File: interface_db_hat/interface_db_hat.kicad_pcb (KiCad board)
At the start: 4 copper layers, 65 x 56 mm, 88 parts, among them J1 GPIO, J10 Conn_02x06_Counter_Clockwise, J2 DF19G-20P-1H52, J3 Conn_02x06_Counter_Clockwise, J4 Conn_Coaxial_Small, J5 Conn_01x04_Pin, J6 Conn_01x04_Pin, J8 Conn_01x03_Pin, J9 Conn_02x06_Counter_Clockwise, Q1 BC817, U1 MAX-M10M-00B, U2 TCA9617ADGKR, U7 MCP23017x-x-SO

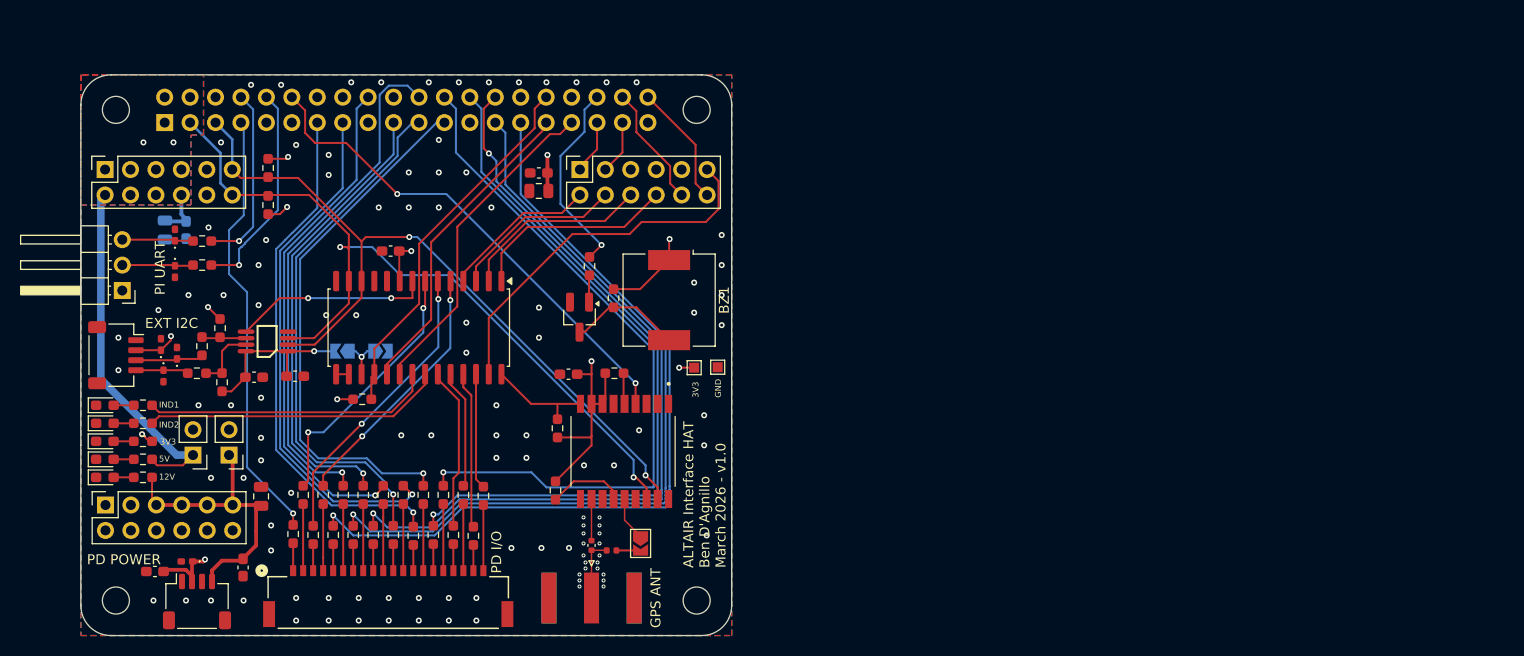
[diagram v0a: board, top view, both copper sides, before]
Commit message: starting interface layout
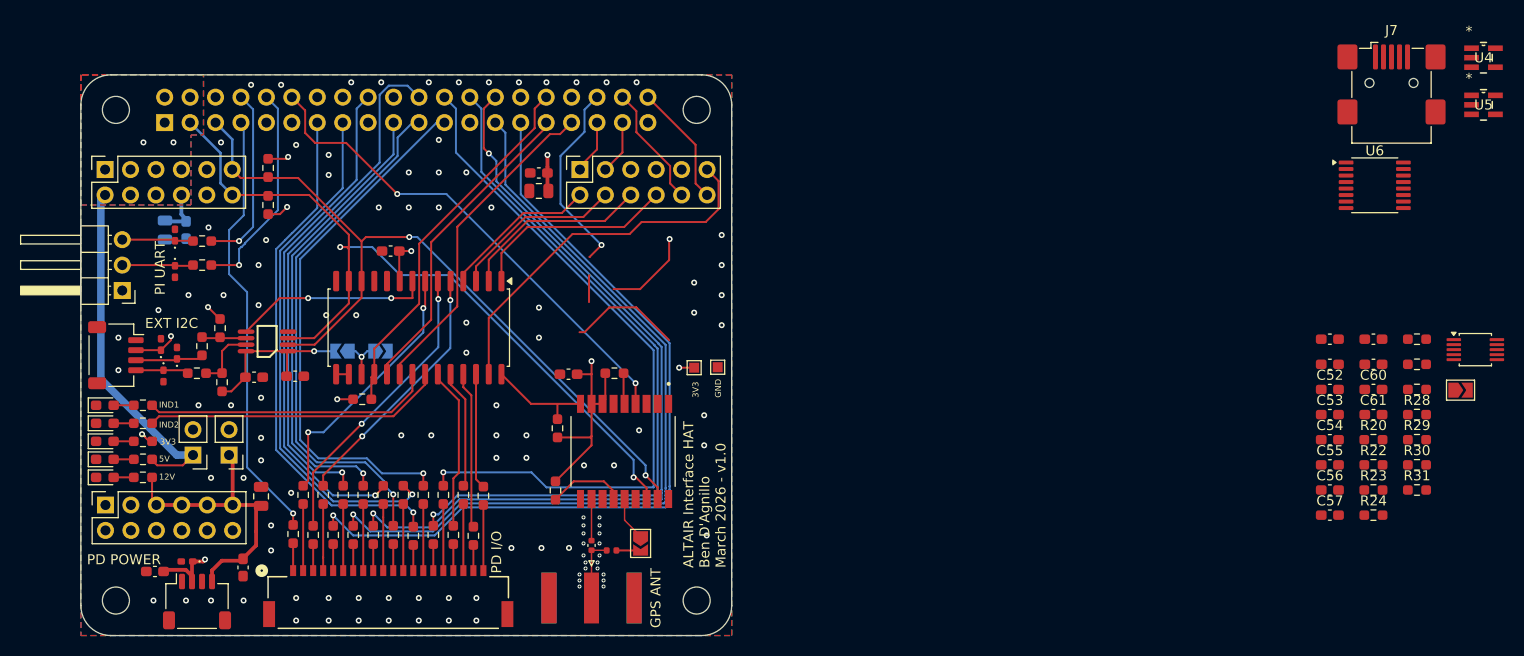
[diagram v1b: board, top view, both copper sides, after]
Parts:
- removed BZ1: Buzzer, Buzzer_Beeper:Buzzer_CUI_CPT-9019S-SMT
- removed Q1: BC817, Package_TO_SOT_SMD:SOT-23_Handsoldering
- removed R15, R17: 330, Resistor_SMD:R_0603_1608Metric_Pad0.98x0.95mm_HandSolder
- added C50: 100nF, Capacitor_SMD:C_0603_1608Metric_Pad1.08x0.95mm_HandSolder, F.Cu at (224.7, 70.4)
- added C51: 100nF, Capacitor_SMD:C_0603_1608Metric_Pad1.08x0.95mm_HandSolder, F.Cu at (224.7, 72.9)
- added C52: 100nF, Capacitor_SMD:C_0603_1608Metric_Pad1.08x0.95mm_HandSolder, F.Cu at (224.7, 75.4)
- added C53: 100nF, Capacitor_SMD:C_0603_1608Metric_Pad1.08x0.95mm_HandSolder, F.Cu at (224.7, 77.9)
- added C54: 1nF, Capacitor_SMD:C_0603_1608Metric_Pad1.08x0.95mm_HandSolder, F.Cu at (224.7, 80.4)
- added C55: 330pF, Capacitor_SMD:C_0603_1608Metric_Pad1.08x0.95mm_HandSolder, F.Cu at (224.7, 83.0)
- added C56: 100pF, Capacitor_SMD:C_0603_1608Metric_Pad1.08x0.95mm_HandSolder, F.Cu at (224.7, 85.5)
- added C57: 33pF, Capacitor_SMD:C_0603_1608Metric_Pad1.08x0.95mm_HandSolder, F.Cu at (224.7, 88.0)
- added C58: 1nF, Capacitor_SMD:C_0603_1608Metric_Pad1.08x0.95mm_HandSolder, F.Cu at (229.1, 70.4)
- added C59: 330pF, Capacitor_SMD:C_0603_1608Metric_Pad1.08x0.95mm_HandSolder, F.Cu at (229.1, 72.9)
- added C60: 100pF, Capacitor_SMD:C_0603_1608Metric_Pad1.08x0.95mm_HandSolder, F.Cu at (229.1, 75.4)
- added C61: 33pF, Capacitor_SMD:C_0603_1608Metric_Pad1.08x0.95mm_HandSolder, F.Cu at (229.1, 77.9)
- added J7: USB_B_Mini, Connector_USB:USB_Mini-B_Wuerth_65100516121_Horizontal, F.Cu at (230.9, 44.8)
- added JP9: SolderJumper_2_Open, Jumper:SolderJumper-2_P1.3mm_Open_TrianglePad1.0x1.5mm, F.Cu at (237.8, 75.5)
- added R20: 50, Resistor_SMD:R_0603_1608Metric_Pad0.98x0.95mm_HandSolder, F.Cu at (229.1, 80.4)
- added R22: 100, Resistor_SMD:R_0603_1608Metric_Pad0.98x0.95mm_HandSolder, F.Cu at (229.1, 83.0)
- added R23: 1k, Resistor_SMD:R_0603_1608Metric_Pad0.98x0.95mm_HandSolder, F.Cu at (229.1, 85.5)
- added R24: 0, Resistor_SMD:R_0603_1608Metric_Pad0.98x0.95mm_HandSolder, F.Cu at (229.1, 88.0)
- added R25: 0, Resistor_SMD:R_0603_1608Metric_Pad0.98x0.95mm_HandSolder, F.Cu at (233.4, 70.4)
- added R26: 10k, Resistor_SMD:R_0603_1608Metric_Pad0.98x0.95mm_HandSolder, F.Cu at (233.4, 72.9)
- added R27: 100k, Resistor_SMD:R_0603_1608Metric_Pad0.98x0.95mm_HandSolder, F.Cu at (233.4, 75.4)
- added R28: 100, Resistor_SMD:R_0603_1608Metric_Pad0.98x0.95mm_HandSolder, F.Cu at (233.4, 77.9)
- added R29: 1k, Resistor_SMD:R_0603_1608Metric_Pad0.98x0.95mm_HandSolder, F.Cu at (233.4, 80.4)
- added R30: 10k, Resistor_SMD:R_0603_1608Metric_Pad0.98x0.95mm_HandSolder, F.Cu at (233.4, 83.0)
- added R31: 100k, Resistor_SMD:R_0603_1608Metric_Pad0.98x0.95mm_HandSolder, F.Cu at (233.4, 85.5)
- added U3: ADS1115IDGS, Package_SO:TSSOP-10_3x3mm_P0.5mm, F.Cu at (239.3, 71.4)
- added U4: OPA320AIDBVR, OPA320:DBV5, F.Cu at (240.1, 42.3)
- added U5: OPA320AIDBVR, OPA320:DBV5, F.Cu at (240.1, 47.0)
- added U6: TMUX1209PWR, Package_SO:TSSOP-16_4.4x5mm_P0.65mm, F.Cu at (229.2, 55.0)
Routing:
- net (no net): track 0.00 -> 14.0 mm
- net Net-(BZ1--): track 11.3 -> 0.00 mm
- net Net-(Q1-B): track 2.71 -> 0.00 mm

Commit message: interface layout done
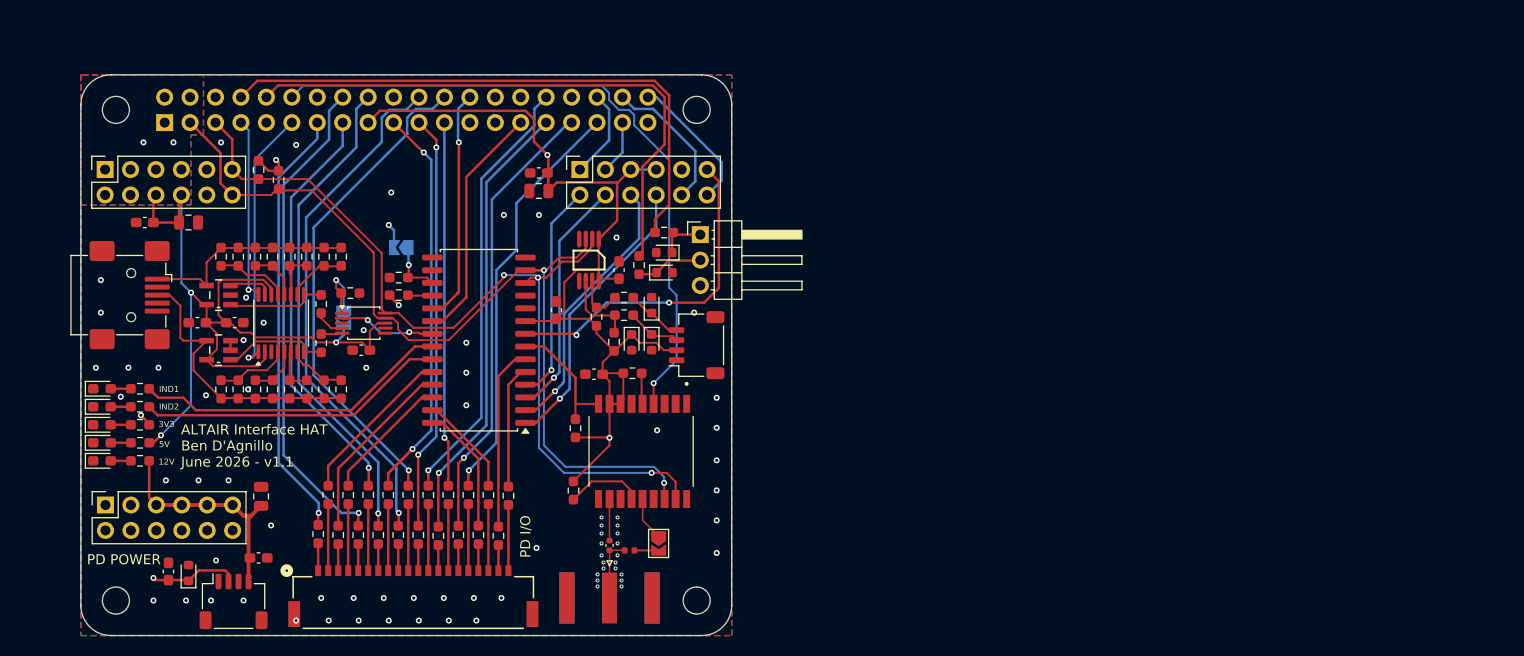
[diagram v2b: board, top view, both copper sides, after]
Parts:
- removed C4, C53: 100nF, Capacitor_SMD:C_0603_1608Metric_Pad1.08x0.95mm_HandSolder
- removed JP8: SolderJumper_2_Open, Jumper:SolderJumper-2_P1.3mm_Open_TrianglePad1.0x1.5mm
- removed TP1, TP2: TestPoint_2Pole, Connector_PinHeader_2.54mm:PinHeader_1x02_P2.54mm_Vertical
- removed TP3, TP4: TestPoint, TestPoint:TestPoint_Pad_1.0x1.0mm
- added R13: 10k, Resistor_SMD:R_0603_1608Metric_Pad0.98x0.95mm_HandSolder, F.Cu at (131.8, 64.2)
- C33, C34: moved to F.Cu
- C54, C55, C56, C57, C58, C59, C60, C61: footprint Capacitor_SMD:C_0603_1608Metric_Pad1.08x0.95mm_HandSolder -> Resistor_SMD:R_0603_1608Metric_Pad0.98x0.95mm_HandSolder
- D10, D36, D37, D38, D47, D48: footprint Diode_SMD:D_0402_1005Metric_Pad0.77x0.64mm_HandSolder -> Diode_SMD:D_0603_1608Metric
- JP9: moved to B.Cu
- moved U4 129.7 mm to (113.8, 71.5), turned to 180 degrees
- moved U5 127.7 mm to (113.8, 66.0), turned to 180 degrees
- moved J7 127.6 mm to (105.0, 66.0), turned to -90 degrees
- moved R28 118.8 mm to (115.7, 62.2), turned to -90 degrees
- moved R29 115.7 mm to (119.1, 62.2), turned to -90 degrees
- moved C58 115.4 mm to (114.0, 62.2), turned to 90 degrees
- moved R30 114.5 mm to (120.9, 62.2), turned to -90 degrees
- moved R22 113.6 mm to (115.7, 75.4), turned to 90 degrees
- moved C50 113.1 mm to (111.6, 68.8), turned to 180 degrees
- moved R26 112.6 mm to (120.9, 75.4), turned to 90 degrees
- moved C59 112.2 mm to (117.4, 62.2), turned to 90 degrees
- moved JP9 111.8 mm to (126.2, 68.3), turned to -90 degrees
- moved U3 111.0 mm to (128.2, 68.8)
- moved C54 110.9 mm to (114.0, 75.4), turned to -90 degrees
- moved R23 110.4 mm to (119.1, 75.4), turned to 90 degrees
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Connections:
- C55 pad 2: /photodiode/RC2_IN -> /photodiode/PDA_ANODE
- C56 pad 2: /photodiode/RC2_IN -> /photodiode/PDA_ANODE
- C57 pad 2: /photodiode/RC2_IN -> /photodiode/PDA_ANODE
- C59 pad 2: /photodiode/RC2_IN -> /photodiode/PDB_ANODE
- C60 pad 2: /photodiode/RC2_IN -> /photodiode/PDB_ANODE
- C61 pad 2: /photodiode/RC2_IN -> /photodiode/PDB_ANODE
- J1 pad 11: /HAT_connections/GPIO17 -> /MUX_A0
- J1 pad 13: /SPI_CS4 -> /INT_SLCTA
- J1 pad 15: /SPI_CS3 -> /~{DRDY1}
- J1 pad 16: /HAT_connections/GPIO23 -> /INT_SLCTB
- J1 pad 18: /STRT2 -> /~{DRDY2}
- J1 pad 22: /~{DRDY1} -> /STRT1
- J1 pad 24: /SPI_CS2 -> /STRT2
- J1 pad 26: /SPI_CS1 -> /EXP_INT_B
- J1 pad 27: /~{DRDY2} -> /HAT_connections/ID_SDA
- J1 pad 28: /STRT1 -> /HAT_connections/ID_SCL
- J1 pad 29: /INT_SLCTB -> /EXP_INT_A
- J1 pad 31: /HAT_connections/EXP_INT_B -> /SPI_CS4
- J1 pad 32: /HAT_connections/GPIO12/PWM0 -> /SPI_CS3
- J1 pad 33: /HAT_connections/EXP_INT_A -> /SPI_CS1
- J1 pad 35: /SERVO_2 -> /SPI_CS2
- J1 pad 36: /BUZZER -> /SERVO_2
- J1 pad 7: /INT_SLCTA -> /MUX_A1
- J7 pad 1: /photodiode/PDA_ANODE -> /photodiode/PDB_ANODE
- J7 pad 3: /photodiode/PDB_ANODE -> /photodiode/PDA_ANODE
- J8 pad 1: GND -> Net-(D48-K)
- J8 pad 3: Net-(D48-K) -> GND
- R23 pad 1: /photodiode/RC2_IN -> /photodiode/PDA_ANODE
- R24 pad 2: /photodiode/PD_OUTA -> /photodiode/PD_OUTB
- R25 pad 1: /photodiode/PD_OUTB -> /photodiode/PD_OUTA
- R26 pad 1: /photodiode/RC2_IN -> /photodiode/PDA_ANODE
- R27 pad 1: /photodiode/RC2_IN -> /photodiode/PDA_ANODE
- R29 pad 1: /photodiode/RC2_IN -> /photodiode/PDB_ANODE
- R30 pad 1: /photodiode/RC2_IN -> /photodiode/PDB_ANODE
- R31 pad 1: /photodiode/RC2_IN -> /photodiode/PDB_ANODE
- R9 pad 1: /HAT_connections/GPIO12/PWM0 -> /HAT_connections/~{IO_EXP_RST}
- U2 pad 5: /HAT_connections/I2CB_EN -> unconnected-(U2-EN-Pad5)
- U3 pad 10: /photodiode/I2C_SCL -> /I2C_SCL
- U3 pad 2: /photodiode/ADC_RDY -> /ADC_RDY
- U3 pad 9: /photodiode/I2C_SDA -> /I2C_SDA
- U6 pad 1: /photodiode/MUX_A0 -> /MUX_A0
- U6 pad 16: /photodiode/MUX_A1 -> /MUX_A1
- U7 pad 18: /HAT_connections/GPIO12/PWM0 -> /HAT_connections/~{IO_EXP_RST}
- U7 pad 19: /HAT_connections/EXP_INT_B -> /EXP_INT_B
- U7 pad 20: /HAT_connections/EXP_INT_A -> /EXP_INT_A
- U7 pad 21: /IND_1 -> /ADC_RDY
- U7 pad 22: /IND_2 -> /IND_1
- U7 pad 23: /IVC_SW_2_SOL -> /IND_2
- U7 pad 24: /IVC_SW_1_SOL -> /~{PD_RESET}
- U7 pad 25: /IVC_SW_1 -> /INT_RST
- U7 pad 26: /IVC_SW_2 -> /INT_HLD
- U7 pad 27: /IND_3 -> /IVC_SW_1_SOL
- U7 pad 28: /~{GPS_RST} -> /IVC_SW_2_SOL
- U7 pad 5: /INT_HLD -> /IVC_SW_2
- U7 pad 6: /INT_RST -> /IVC_SW_1
- U7 pad 7: /~{PD_RESET} -> /~{GPS_RST}
- U7 pad 8: /HAT_connections/I2CB_EN -> /IND_3
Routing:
- net +3V3: track 68.6 -> 120.6 mm, vias 12 -> 7
- net /HAT_connections/GPIO14/TXD0: track 18.2 -> 58.3 mm, vias 1 -> 0
- net /HAT_connections/GPIO12/PWM0: track 37.4 -> 0.00 mm
- net /HAT_connections/GPIO15/RXD0: track 21.7 -> 57.7 mm, vias 1 -> 0
- net /HAT_connections/EXP_INT_A: track 32.8 -> 0.00 mm
- net /HAT_connections/EXP_INT_B: track 31.7 -> 0.00 mm
- net /INT_SLCTB: track 81.0 -> 49.4 mm
- net /~{DRDY2}: track 79.2 -> 49.0 mm
- net /SPI_CS2: track 70.6 -> 41.6 mm
- net /photodiode/PDA_ANODE: track 0.00 -> 28.1 mm
- net /STRT1: track 79.8 -> 52.3 mm, vias 2 -> 1
- net /SPI_CS1: track 71.9 -> 45.1 mm
- net /MUX_A0: track 0.00 -> 26.6 mm, vias 0 -> 1
- net /EXP_INT_A: track 0.00 -> 24.1 mm
- net /EXP_INT_B: track 0.00 -> 23.4 mm, vias 0 -> 1
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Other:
- board text added: "ALTAIR Interface HAT Ben D'Agnillo June 2026 - v1.1"
- board text removed: "ALTAIR Interface HAT Ben D'Agnillo March 2026 - v1.0"
- board text removed: "EXT I2C"
- board text removed: "GND"
- board text removed: "GPS ANT"
- board text removed: "PI UART"

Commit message: fixed interface schematic
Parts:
- C54, C55, C56, C57, C58, C59, C60, C61: footprint Resistor_SMD:R_0603_1608Metric_Pad0.98x0.95mm_HandSolder -> Capacitor_SMD:C_0603_1608Metric_Pad1.08x0.95mm_HandSolder

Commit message: jlc order
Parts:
- removed C50, C51, C52: 100nF, Capacitor_SMD:C_0603_1608Metric_Pad1.08x0.95mm_HandSolder
- removed C54, C58: 1nF, Capacitor_SMD:C_0603_1608Metric_Pad1.08x0.95mm_HandSolder
- removed C55, C59: 330pF, Capacitor_SMD:C_0603_1608Metric_Pad1.08x0.95mm_HandSolder
- removed C56, C60: 100pF, Capacitor_SMD:C_0603_1608Metric_Pad1.08x0.95mm_HandSolder
- removed C57, C61: 33pF, Capacitor_SMD:C_0603_1608Metric_Pad1.08x0.95mm_HandSolder
- removed JP9: SolderJumper_2_Open, Jumper:SolderJumper-2_P1.3mm_Open_TrianglePad1.0x1.5mm
- removed R22, R28: 100, Resistor_SMD:R_0603_1608Metric_Pad0.98x0.95mm_HandSolder
- removed R23, R29: 1k, Resistor_SMD:R_0603_1608Metric_Pad0.98x0.95mm_HandSolder
- removed R24, R25: 0, Resistor_SMD:R_0603_1608Metric_Pad0.98x0.95mm_HandSolder
- removed R26, R30: 10k, Resistor_SMD:R_0603_1608Metric_Pad0.98x0.95mm_HandSolder
- removed R27, R31: 100k, Resistor_SMD:R_0603_1608Metric_Pad0.98x0.95mm_HandSolder
- removed U3: ADS1115IDGS, Package_SO:TSSOP-10_3x3mm_P0.5mm
- removed U4, U5: OPA320AIDBVR, OPA320:DBV5
- removed U6: TMUX1209PWR, Package_SO:TSSOP-16_4.4x5mm_P0.65mm
- added J11: Conn_01x06_Pin, Connector_JST:JST_GH_SM06B-GHS-TB_1x06-1MP_P1.25mm_Horizontal, F.Cu at (104.0, 76.8)
- added R1: 33, Resistor_SMD:R_0603_1608Metric, F.Cu at (109.2, 79.9)
- added R15: 33, Resistor_SMD:R_0603_1608Metric, F.Cu at (112.2, 76.1)
- added R17: 33, Resistor_SMD:R_0603_1608Metric, F.Cu at (109.2, 67.4)
- added R18: 33, Resistor_SMD:R_0603_1608Metric, F.Cu at (112.2, 66.1)
- added R19: 33, Resistor_SMD:R_0603_1608Metric, F.Cu at (109.2, 64.9)
- added R5: 33, Resistor_SMD:R_0603_1608Metric, F.Cu at (112.2, 78.6)
- added R6: 33, Resistor_SMD:R_0603_1608Metric, F.Cu at (109.2, 77.4)
- J7: value USB_B_Mini -> Conn_01x06_Pin; footprint Connector_USB:USB_Mini-B_Wuerth_65100516121_Horizontal -> Connector_JST:JST_GH_SM06B-GHS-TB_1x06-1MP_P1.25mm_Horizontal
- R20: value 50 -> 33; footprint Resistor_SMD:R_0603_1608Metric_Pad0.98x0.95mm_HandSolder -> Resistor_SMD:R_0603_1608Metric
- moved R10 44.4 mm to (145.8, 59.4)
- moved D2 44.4 mm to (142.0, 59.4)
- moved D3 27.6 mm to (118.8, 58.8), turned to 180 degrees
- moved R14 25.2 mm to (130.8, 71.6)
- moved R16 25.2 mm to (130.8, 73.4)
- moved D6 25.2 mm to (127.0, 71.6)
- moved D7 25.2 mm to (127.0, 73.4)
- moved R11 23.8 mm to (115.0, 58.8), turned to 0 degrees
- moved R20 14.8 mm to (112.2, 63.6)
- moved C33 3.01 mm to (109.0, 60.1), turned to 90 degrees
- moved J7 2.03 mm to (104.0, 64.2)
- moved D4 1.67 mm to (102.4, 84.2)
- moved R12 1.67 mm to (106.2, 84.2)
- moved C34 1.54 mm to (111.4, 60.1), turned to -90 degrees
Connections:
- J7 pad 1: /photodiode/PDB_ANODE -> +5V
- J7 pad 3: /photodiode/PDA_ANODE -> Net-(J7-Pin_3)
- J7 pad 4: GND -> Net-(J7-Pin_4)
- J7 pad 5: GND -> Net-(J7-Pin_5)
- R20 pad 1: GND -> /SPI_MISO
- R20 pad 2: Net-(JP9-A) -> Net-(J7-Pin_3)
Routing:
- net /SPI_MOSI: track 43.0 -> 101.8 mm, vias 2 -> 3
- net +5V: track 85.7 -> 27.1 mm, vias 5 -> 2
- net /SPI_SCLK: track 36.4 -> 90.5 mm, vias 1 -> 3
- net /SPI_MISO: track 41.7 -> 95.1 mm, vias 2 -> 4
- net /IND_1: track 31.8 -> 3.58 mm
- net /photodiode/PDA_ANODE: track 28.1 -> 0.00 mm
- net /IND_2: track 30.9 -> 3.80 mm
- net /photodiode/PDB_ANODE: track 21.5 -> 0.00 mm
- net /MUX_A1: track 18.2 -> 33.4 mm
- net /photodiode/PD_OUTA: track 10.7 -> 0.00 mm
- net /photodiode/PD_OUTB: track 10.0 -> 0.00 mm
- net /ADC_RDY: track 9.73 -> 0.00 mm, vias 2 -> 0
- net /photodiode/RC1A: track 7.30 -> 0.00 mm
- net /photodiode/RC1B: track 7.27 -> 0.00 mm
- net Net-(JP9-A): track 6.91 -> 0.00 mm, vias 1 -> 0
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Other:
- board text added: "ALTAIR Interface HAT Ben D'Agnillo June 2026 - v1.2"
- board text removed: "ALTAIR Interface HAT Ben D'Agnillo June 2026 - v1.1"

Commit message: still trying to order. last minute fixes
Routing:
- net +3V3: track 119.2 -> 122.9 mm
